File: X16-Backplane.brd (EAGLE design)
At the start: 160 x 100 mm, 0 parts

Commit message: 9/27/2023
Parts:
- added J1: CONN_PXC-8-RA-1778683, X16_Backplane:PXC-8-RA-1778683
- added J2: CONN_ET60S-D04-3-08-D04-X-R1-S, X16_Backplane:SAMTEC_ET60S-D04-3-08-D04-X-R1-S
- added J3: CONN_HTST-108-04-X-D-RAJ, X16_Backplane:SAMTEC-HTST-108-04-X-D-RA
- added U$1: CONN_BACKPLANE_ESC_CONTROLLERBKP, X16_Backplane:BACKPLANE_CONNECTORS_BKP
- added U$2, U$3, U$4: CONN_BACKPLANE_ESC_ADAPTER, X16_Backplane:CONN_BACKPLANE_ESC_ADAPTER
- added U1: TRANS_ULN2003AD, X16_Backplane:16-SOIC
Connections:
- new net 12L_GND: J3.5
- new net 12V: U$2.12V@10, U$2.12V@11, U$2.12V@12, U$2.12V@3, U$2.12V@4, U$2.12V@5, U$2.12V@6, U$2.12V@7, U$2.12V@8, U$2.12V@9, U$3.12V@10, U$3.12V@11, U$3.12V@12, U$3.12V@3, U$3.12V@4, U$3.12V@5, U$3.12V@6, U$3.12V@7, U$3.12V@8, U$3.12V@9, U$4.12V@10, U$4.12V@11, U$4.12V@12, U$4.12V@3, U$4.12V@4, U$4.12V@5, U$4.12V@6, U$4.12V@7, U$4.12V@8, U$4.12V@9
- new net 12V_GND: U$2.GND@1, U$2.GND@10, U$2.GND@2, U$2.GND@3, U$2.GND@4, U$2.GND@5, U$2.GND@6, U$2.GND@7, U$2.GND@8, U$2.GND@9, U$3.GND@1, U$3.GND@10, U$3.GND@2, U$3.GND@3, U$3.GND@4, U$3.GND@5, U$3.GND@6, U$3.GND@7, U$3.GND@8, U$3.GND@9, U$4.GND@1, U$4.GND@10, U$4.GND@2, U$4.GND@3, U$4.GND@4, U$4.GND@5, U$4.GND@6, U$4.GND@7, U$4.GND@8, U$4.GND@9
- new net 12V_L: J1.1, J1.2, U1.9
- new net 3V3: J3.11
- new net 5V: J3.7
- new net GND: J3.9, U1.8
- new net GPIO1: J3.2, U1.1
- new net GPIO2: J3.4, U1.2
- new net GPIO3: J3.6, U1.3
- new net GPIO4: J3.8, U1.4
- new net GPIO5: J3.10, U1.5
- new net GPIO6: J3.12, U1.6
- new net N$10: U$2.PWM3
- new net N$11: U$2.NC@1, U$2.NC@2, U$2.NC@3, U$2.NC@4, U$2.NC@5, U$2.NC@6
- new net N$12: U$3.PWM0
- new net N$13: U$3.PWM1
- new net N$14: U$3.PWM2
- new net N$15: U$3.PWM3
- new net N$16: U$3.NC@1, U$3.NC@2, U$3.NC@3, U$3.NC@4, U$3.NC@5, U$3.NC@6
- new net N$17: U$4.PWM0
- new net N$18: U$4.PWM1
- new net N$19: U$4.PWM2
- new net N$20: U$4.PWM3
- new net N$21: U$4.NC@1, U$4.NC@2, U$4.NC@3, U$4.NC@4, U$4.NC@5, U$4.NC@6
- new net N$23: U1.10
- new net N$30: U1.7
- new net N$7: U$2.PWM0
- new net N$8: U$2.PWM1
- new net N$9: U$2.PWM2
- new net P01: J2.P01_1, J2.P01_10, J2.P01_2, J2.P01_3, J2.P01_4, J2.P01_5, J2.P01_6, J2.P01_7, J2.P01_8, J2.P01_9
- new net P02: J2.P02_1, J2.P02_10, J2.P02_2, J2.P02_3, J2.P02_4, J2.P02_5, J2.P02_6, J2.P02_7, J2.P02_8, J2.P02_9
- new net P03: J2.P03_1, J2.P03_10, J2.P03_2, J2.P03_3, J2.P03_4, J2.P03_5, J2.P03_6, J2.P03_7, J2.P03_8, J2.P03_9
- new net P04: J2.P04_1, J2.P04_10, J2.P04_2, J2.P04_3, J2.P04_4, J2.P04_5, J2.P04_6, J2.P04_7, J2.P04_8, J2.P04_9
- new net P05: J2.P05_1, J2.P05_10, J2.P05_2, J2.P05_3, J2.P05_4, J2.P05_5, J2.P05_6, J2.P05_7, J2.P05_8, J2.P05_9
- new net P06: J2.P06_1, J2.P06_10, J2.P06_2, J2.P06_3, J2.P06_4, J2.P06_5, J2.P06_6, J2.P06_7, J2.P06_8, J2.P06_9
- new net P07: J2.P07_1, J2.P07_10, J2.P07_2, J2.P07_3, J2.P07_4, J2.P07_5, J2.P07_6, J2.P07_7, J2.P07_8, J2.P07_9
- new net P08: J2.P08_1, J2.P08_10, J2.P08_2, J2.P08_3, J2.P08_4, J2.P08_5, J2.P08_6, J2.P08_7, J2.P08_8, J2.P08_9
- new net SOL1_1: J1.3, U1.16
- new net SOL2_1: J1.4, U1.15
- new net SOL3_1: J1.5, U1.14
- new net SOL4_1: J1.6, U1.13
- new net SOL5_1: J1.7, U1.12
- new net SOL6_1: J1.8, U1.11
- new net SPI1: J3.13
- new net SPI2: J3.15
- new net SPI3: J3.14
- new net SPI4: J3.16

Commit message: 9/27/2023
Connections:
- net SPI1 renamed SPI_MOSI
- net SPI2 renamed SPI_MISO
- net SPI3 renamed SPI_SCLK
- net SPI4 renamed SPI_SS/CS
- new net ESC_ID: U$1.12
- new net N$25: U$1.5
- new net N$26: U$1.7
- new net N$4: U$1.8
- new net NRST: U$1.6
- new net SWCLK: U$1.11
- new net SWDIO: U$1.9
- net 3V3: now also U$1.1, U$1.2, U$1.3, U$1.4
- net GND: now also U$1.10
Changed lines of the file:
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@@
 <contactref element="J3" pad="9"/>
 <contactref element="U1" pad="8"/>
+<contactref element="U$1" pad="10"/>
+<wire x1="-75.2" y1="-19.86" x2="-78.74" y2="-44.196" width="0" layer="19" extent="1-1"/>
 <wire x1="-101.535" y1="-186.055" x2="-78.74" y2="-44.196" width="0" layer="19" extent="1-1"/>
 </signal>
 <signal name="3V3">
 <contactref element="J3" pad="11"/>
+<contactref element="U$1" pad="2"/>
+<contactref element="U$1" pad="4"/>
+<contactref element="U$1" pad="1"/>
+<contactref element="U$1" pad="3"/>
+<wire x1="-77.2" y1="-27.86" x2="-81.28" y2="-44.196" width="0" layer="19" extent="1-1"/>
+<wire x1="-77.2" y1="-25.86" x2="-77.2" y2="-27.86" width="0" layer="19" extent="1-1"/>
+<wire x1="-75.2" y1="-27.86" x2="-77.2" y2="-27.86" width="0" layer="19" extent="1-1"/>
+<wire x1="-75.2" y1="-25.86" x2="-77.2" y2="-25.86" width="0" layer="19" extent="1-1"/>
 </signal>
-<signal name="SPI1">
+<signal name="SPI_MOSI">
 <contactref element="J3" pad="13"/>
 </signal>
-<signal name="SPI2">
+<signal name="SPI_MISO">
 <contactref element="J3" pad="15"/>
 </signal>
-<signal name="SPI3">
+<signal name="SPI_SCLK">
 <contactref element="J3" pad="14"/>
 </signal>
-<signal name="SPI4">
+<signal name="SPI_SS/CS">
 <contactref element="J3" pad="16"/>
 </signal>
@@
 <contactref element="U1" pad="7"/>
 </signal>
+<signal name="NRST">
+<contactref element="U$1" pad="6"/>
+</signal>
+<signal name="N$4">
+<contactref element="U$1" pad="8"/>
+</signal>
+<signal name="ESC_ID">
+<contactref element="U$1" pad="12"/>
+</signal>
+<signal name="N$25">
+<contactref element="U$1" pad="5"/>
+</signal>
+<signal name="N$26">
+<contactref element="U$1" pad="7"/>
+</signal>
+<signal name="SWDIO">
+<contactref element="U$1" pad="9"/>
+</signal>
+<signal name="SWCLK">
+<contactref element="U$1" pad="11"/>
+</signal>
 </signals>

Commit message: 09/30/2023
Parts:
- added D1, D2, D3: (no value), SparkFun-LED:LED-0603
- added R1, R2, R3: (no value), SparkFun-Resistors:0603
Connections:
- net N$10 renamed PWMA3
- net N$12 renamed PWMB0
- net N$13 renamed PWMB1
- net N$14 renamed PWMB2
- net N$15 renamed PWMB3
- net N$17 renamed PWMC0
- net N$18 renamed PWMC1
- net N$19 renamed PWMC2
- net N$20 renamed PWMC3
- net N$7 renamed PWMA0
- net N$8 renamed PWMA1
- net N$9 renamed PWMA2
- removed net ESC_ID: U$1.12
- removed net N$25: U$1.5
- removed net N$26: U$1.7
- removed net N$4: U$1.8
- removed net P01: J2.P01_1, J2.P01_10, J2.P01_2, J2.P01_3, J2.P01_4, J2.P01_5, J2.P01_6, J2.P01_7, J2.P01_8, J2.P01_9
- removed net P02: J2.P02_1, J2.P02_10, J2.P02_2, J2.P02_3, J2.P02_4, J2.P02_5, J2.P02_6, J2.P02_7, J2.P02_8, J2.P02_9
- removed net P03: J2.P03_1, J2.P03_10, J2.P03_2, J2.P03_3, J2.P03_4, J2.P03_5, J2.P03_6, J2.P03_7, J2.P03_8, J2.P03_9
- removed net P04: J2.P04_1, J2.P04_10, J2.P04_2, J2.P04_3, J2.P04_4, J2.P04_5, J2.P04_6, J2.P04_7, J2.P04_8, J2.P04_9
- removed net P05: J2.P05_1, J2.P05_10, J2.P05_2, J2.P05_3, J2.P05_4, J2.P05_5, J2.P05_6, J2.P05_7, J2.P05_8, J2.P05_9
- removed net P06: J2.P06_1, J2.P06_10, J2.P06_2, J2.P06_3, J2.P06_4, J2.P06_5, J2.P06_6, J2.P06_7, J2.P06_8, J2.P06_9
- removed net P07: J2.P07_1, J2.P07_10, J2.P07_2, J2.P07_3, J2.P07_4, J2.P07_5, J2.P07_6, J2.P07_7, J2.P07_8, J2.P07_9
- removed net P08: J2.P08_1, J2.P08_10, J2.P08_2, J2.P08_3, J2.P08_4, J2.P08_5, J2.P08_6, J2.P08_7, J2.P08_8, J2.P08_9
- removed net SPI_MISO: J3.15
- removed net SPI_MOSI: J3.13
- removed net SPI_SCLK: J3.14
- removed net SPI_SS/CS: J3.16
- new net ALERT1: J2.23
- new net ALERT2: J2.24
- new net C2_1: J2.20
- new net C2_2: J2.21
- new net CLK: J2.22
- new net DATA: J2.19
- new net MISO: J3.15, U$1.7
- new net MOSI: J3.13, U$1.5
- new net N$1: D1.C, R1.2
- new net N$5: D2.C, R2.2
- new net N$8: D3.C, R3.2
- new net SCLK: J3.14, U$1.8
- new net SS/CS: J3.16, U$1.10
- net 12L_GND: now also J2.09
- net 12V: now also D1.A, D2.A, D3.A, J2.17, J2.P05_1, J2.P05_10, J2.P05_2, J2.P05_3, J2.P05_4, J2.P05_5, J2.P05_6, J2.P05_7, J2.P05_8, J2.P05_9, J2.P06_1, J2.P06_10, J2.P06_2, J2.P06_3, J2.P06_4, J2.P06_5, J2.P06_6, J2.P06_7, J2.P06_8, J2.P06_9, J2.P07_1, J2.P07_10, J2.P07_2, J2.P07_3, J2.P07_4, J2.P07_5, J2.P07_6, J2.P07_7, J2.P07_8, J2.P07_9, J2.P08_1, J2.P08_10, J2.P08_2, J2.P08_3, J2.P08_4, J2.P08_5, J2.P08_6, J2.P08_7, J2.P08_8, J2.P08_9
- net 12V_L: now also J2.06
- net 3V3: now also J2.04
- net 5V: now also J2.03
- net GND: now also J2.01, J2.05, J2.P01_1, J2.P01_10, J2.P01_2, J2.P01_3, J2.P01_4, J2.P01_5, J2.P01_6, J2.P01_7, J2.P01_8, J2.P01_9, J2.P02_1, J2.P02_10, J2.P02_2, J2.P02_3, J2.P02_4, J2.P02_5, J2.P02_6, J2.P02_7, J2.P02_8, J2.P02_9, J2.P03_1, J2.P03_10, J2.P03_2, J2.P03_3, J2.P03_4, J2.P03_5, J2.P03_6, J2.P03_7, J2.P03_8, J2.P03_9, J2.P04_1, J2.P04_10, J2.P04_2, J2.P04_3, J2.P04_4, J2.P04_5, J2.P04_6, J2.P04_7, J2.P04_8, J2.P04_9, R1.1, R2.1, R3.1, U$1.12; no longer U$1.10

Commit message: 9/30/2023
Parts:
- removed D3: (no value), SparkFun-LED:LED-0603
- removed R3: (no value), SparkFun-Resistors:0603
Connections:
- removed net 12L_GND: J2.09, J3.5
- removed net ALERT1: J2.23
- removed net ALERT2: J2.24
- removed net C2_1: J2.20
- removed net C2_2: J2.21
- removed net CLK: J2.22
- removed net DATA: J2.19
- removed net N$8: D3.C, R3.2
- removed net NRST: U$1.6
- removed net SWDIO: U$1.9
- net 12V: now also J2.P01_1, J2.P01_10, J2.P01_2, J2.P01_3, J2.P01_4, J2.P01_5, J2.P01_6, J2.P01_7, J2.P01_8, J2.P01_9, J2.P02_1, J2.P02_10, J2.P02_2, J2.P02_3, J2.P02_4, J2.P02_5, J2.P02_6, J2.P02_7, J2.P02_8, J2.P02_9; no longer D3.A, J2.17, J2.P05_1, J2.P05_10, J2.P05_2, J2.P05_3, J2.P05_4, J2.P05_5, J2.P05_6, J2.P05_7, J2.P05_8, J2.P05_9, J2.P06_1, J2.P06_10, J2.P06_2, J2.P06_3, J2.P06_4, J2.P06_5, J2.P06_6, J2.P06_7, J2.P06_8, J2.P06_9, J2.P07_1, J2.P07_10, J2.P07_2, J2.P07_3, J2.P07_4, J2.P07_5, J2.P07_6, J2.P07_7, J2.P07_8, J2.P07_9, J2.P08_1, J2.P08_10, J2.P08_2, J2.P08_3, J2.P08_4, J2.P08_5, J2.P08_6, J2.P08_7, J2.P08_8, J2.P08_9
- net 12V_GND: now also J2.P03_1, J2.P03_10, J2.P03_2, J2.P03_3, J2.P03_4, J2.P03_5, J2.P03_6, J2.P03_7, J2.P03_8, J2.P03_9, J2.P04_1, J2.P04_10, J2.P04_2, J2.P04_3, J2.P04_4, J2.P04_5, J2.P04_6, J2.P04_7, J2.P04_8, J2.P04_9
- net 12V_L: no longer J2.06
- net 3V3: no longer J2.04, U$1.1, U$1.2, U$1.3, U$1.4
- net 5V: now also J2.P07_1, J2.P07_10, J2.P07_2, J2.P07_3, J2.P07_4, J2.P07_5, J2.P07_6, J2.P07_7, J2.P07_8, J2.P07_9, J2.P08_1, J2.P08_10, J2.P08_2, J2.P08_3, J2.P08_4, J2.P08_5, J2.P08_6, J2.P08_7, J2.P08_8, J2.P08_9, U$1.1, U$1.2, U$1.3, U$1.4; no longer J2.03
- net GND: now also J2.P05_1, J2.P05_10, J2.P05_2, J2.P05_3, J2.P05_4, J2.P05_5, J2.P05_6, J2.P05_7, J2.P05_8, J2.P05_9, J2.P06_1, J2.P06_10, J2.P06_2, J2.P06_3, J2.P06_4, J2.P06_5, J2.P06_6, J2.P06_7, J2.P06_8, J2.P06_9; no longer J2.01, J2.05, J2.P01_1, J2.P01_10, J2.P01_2, J2.P01_3, J2.P01_4, J2.P01_5, J2.P01_6, J2.P01_7, J2.P01_8, J2.P01_9, J2.P02_1, J2.P02_10, J2.P02_2, J2.P02_3, J2.P02_4, J2.P02_5, J2.P02_6, J2.P02_7, J2.P02_8, J2.P02_9, J2.P03_1, J2.P03_10, J2.P03_2, J2.P03_3, J2.P03_4, J2.P03_5, J2.P03_6, J2.P03_7, J2.P03_8, J2.P03_9, J2.P04_1, J2.P04_10, J2.P04_2, J2.P04_3, J2.P04_4, J2.P04_5, J2.P04_6, J2.P04_7, J2.P04_8, J2.P04_9, R3.1

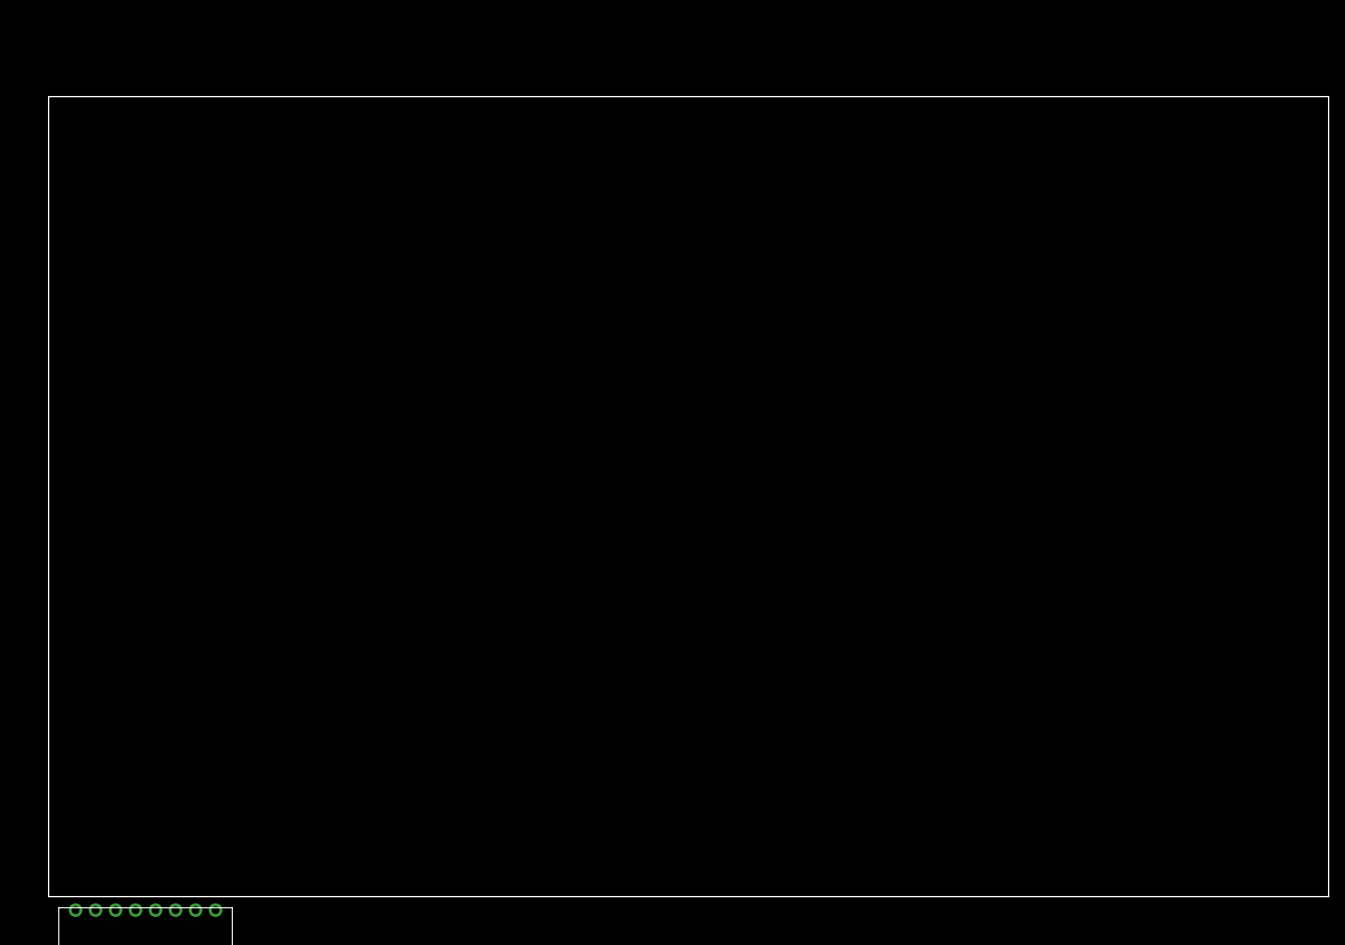
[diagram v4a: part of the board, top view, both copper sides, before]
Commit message: Added board dimensions and removed unneeded files
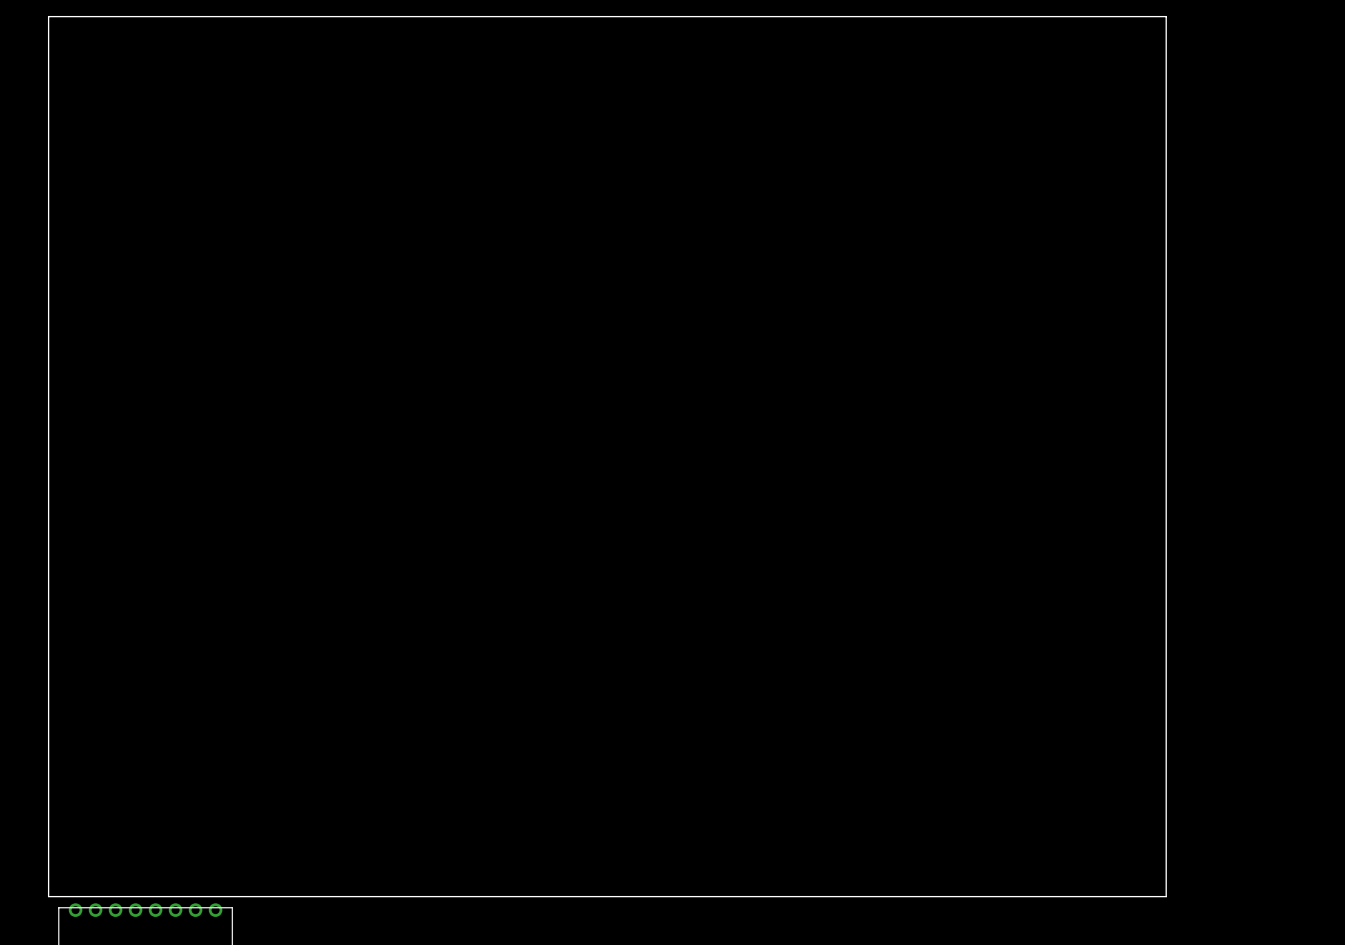
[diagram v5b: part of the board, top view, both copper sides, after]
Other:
- board size 160 x 100 mm -> 139.7 x 110 mm
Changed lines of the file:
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@@
 <setting verticaltext="up"/>
 </settings>
-<grid distance="50" unitdist="mil" unit="mm" style="lines" multiple="1" display="yes" altdistance="5" altunitdist="mil" altunit="mm"/>
+<grid distance="1" unitdist="mm" unit="mm" style="lines" multiple="1" display="yes" altdistance="0.1" altunitdist="mm" altunit="mm"/>
 <layers>
 <layer number="1" name="Top" color="4" fill="1" visible="yes" active="yes"/>
@@
 <board>
 <plain>
-<wire x1="0" y1="0" x2="160" y2="0" width="0.1524" layer="20"/>
-<wire x1="0" y1="0" x2="0" y2="100" width="0.1524" layer="20"/>
-<wire x1="160" y1="0" x2="160" y2="100" width="0.1524" layer="20"/>
-<wire x1="0" y1="100" x2="160" y2="100" width="0.1524" layer="20"/>
+<wire x1="0" y1="0" x2="139.7" y2="0" width="0.1524" layer="20"/>
+<wire x1="0" y1="0" x2="0" y2="110" width="0.1524" layer="20"/>
+<wire x1="139.7" y1="0" x2="139.7" y2="110" width="0.1524" layer="20"/>
+<wire x1="0" y1="110" x2="139.7" y2="110" width="0.1524" layer="20"/>
 </plain>
 <attributes>

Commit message: schematic_complete?
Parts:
- J3: value CONN_HTST-108-04-X-D-RAJ -> SAMTEC-HTST-110-04-X-D-RAJ; device X16_Backplane:SAMTEC-HTST-108-04-X-D-RA -> SAMTEC-HTST-110-04-X-D-RA:SAMTEC-HTST-110-04-X-D-RA
- moved J3 169.0 mm to (-83.0, -221.0)
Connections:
- removed net 3V3: J3.11
- removed net GPIO5: J3.10, U1.5
- removed net GPIO6: J3.12, U1.6
- removed net N$23: U1.10
- removed net N$30: U1.7
- removed net SOL5_1: J1.7, U1.12
- removed net SOL6_1: J1.8, U1.11
- removed net SS/CS: J3.16, U$1.10
- removed net SWCLK: U$1.11
- new net CS: J3.20, U$1.11
- new net CTRL: J2.17, J3.7
- new net DGND: J2.18, J3.9
- new net PWM1: U$1.6
- new net PWM2: U$1.8
- new net PWM3: U$1.10
- new net PWM4: U$1.12
- new net SA0: J2.23, J3.19
- new net SA1: J2.22, J3.17
- new net SALERT: J2.20, J3.13
- new net SCL: J2.21, J3.15
- new net SDA: J2.19, J3.11
- net 5V: now also J3.1; no longer J3.7, U$1.2, U$1.4
- net GND: now also J1.7, J1.8, J3.3, U$1.2, U$1.4; no longer J3.9, U$1.12
- net MISO: now also J3.14, U$1.5; no longer J3.15, U$1.7
- net MOSI: now also J3.16, U$1.7; no longer J3.13, U$1.5
- net SCLK: now also J3.18, U$1.9; no longer J3.14, U$1.8
